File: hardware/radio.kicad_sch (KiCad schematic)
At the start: 25 parts, among them J1 105450-0101, J2 Conn_01x02, J3 Conn_01x02, U1 TP4056, U2 ESP32-WROOM-32, U3 TPS5432, U4 MAX98357

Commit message: schematic
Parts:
- added C13, C15, C16: 100n, Capacitor_SMD:C_0603_1608Metric, symbol Device:C
- added C14: 10u, Capacitor_SMD:C_1206_3216Metric, symbol Device:C
- added J4: Conn_01x04, Connector_PinHeader_2.54mm:PinHeader_1x04_P2.54mm_Vertical, symbol Connector_Generic:Conn_01x04
- added Q1: Q_PMOS_DGS, Package_TO_SOT_SMD:SOT-23, symbol Device:Q_PMOS_DGS
- added Q2: Q_NMOS_DGS, Package_TO_SOT_SMD:SOT-23, symbol Device:Q_NMOS_DGS
- added R5, R8: 10k, Resistor_SMD:R_0603_1608Metric, symbol Device:R
- added R6: 100k, Resistor_SMD:R_0603_1608Metric, symbol Device:R
- added R7: 330k, Resistor_SMD:R_0603_1608Metric, symbol Device:R
- added SW1: SW_BOOT, symbol Switch:SW_Push
- added SW2: SW_RST, symbol Switch:SW_Push
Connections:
- net +3V3: now also C13.2, C14.2, J4.1 (Pin_1), R5.1
- net +BATT: now also Q1.3 (S), R8.1
- net -BATT: now also C13.1, C14.1, C15.1, C16.2, J4.4 (Pin_4), Q2.3 (S), R7.2, SW1.2, SW2.1
- net at U2.25 (IO0): now also C16.1, SW1.1
- net at U2.3 (EN): now also C15.2, R5.2, SW2.2
- net at U2.34 (RXD0/IO3): now also J4.3 (Pin_3)
- net at U2.35 (TXD0/IO1): now also J4.2 (Pin_2)
- new net: Q1.1 (D), R6.1
- new net: Q1.2 (G), Q2.1 (D), R8.2
- new net ADC IN: R6.2, R7.1
- new net ADC_ENABLE: Q2.2 (G)
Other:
- note added: "ADC circuit to prevent leakage current through the resistor divider. Divider reduces the maximum voltage from 4,2 V to ~3,2 V"
- note added: "TODO: * SHUTDOWN CIRCUIT * CONNECT DISPLAY AND DAC/AMP TO ESP32 * CONNECT USB TO ESP32, ADD CC RESISTORS * ADD BUTTONS, ROTARY ENCODER"
- note added: "UART"
- moved on the sheet: C10, C9, DISP1, J3, U2, U4

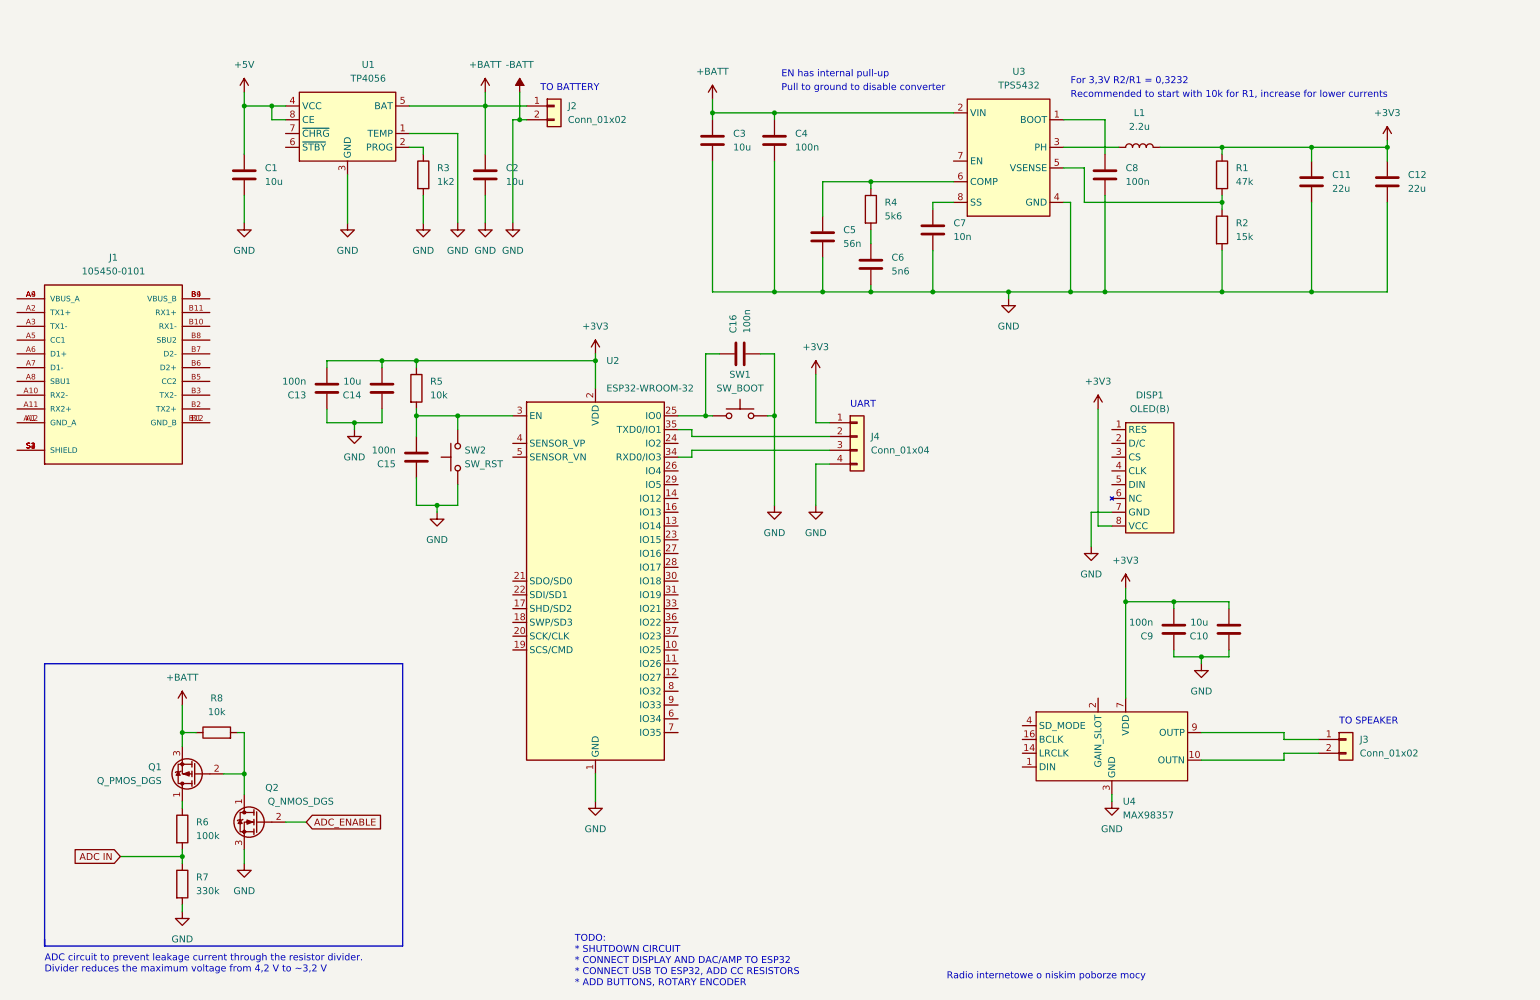
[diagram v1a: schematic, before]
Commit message: added to schematic: rotary encoder, buttons, USB-C receptacle CC resistors
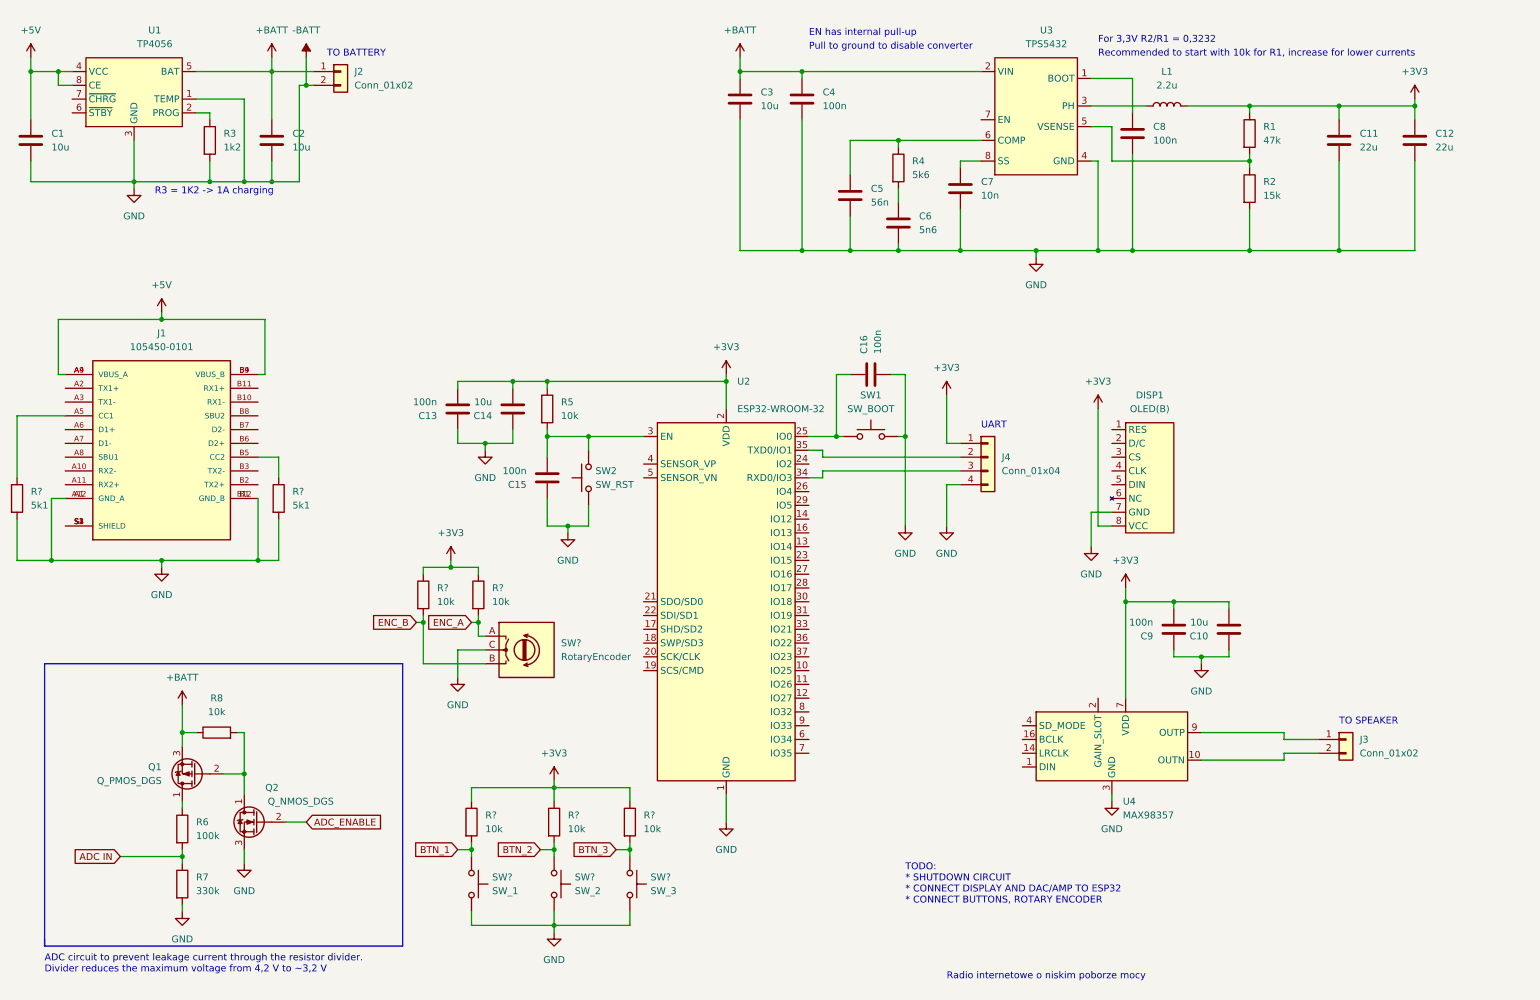
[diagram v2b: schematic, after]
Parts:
- added R? (x5): 10k, Resistor_SMD:R_0603_1608Metric, symbol Device:R
- added R? (x2): 5k1, Resistor_SMD:R_0603_1608Metric, symbol Device:R
- added SW?: SW_1, symbol Switch:SW_Push
- added SW?: RotaryEncoder, symbol Device:RotaryEncoder
- added SW?: SW_2, symbol Switch:SW_Push
- added SW?: SW_3, symbol Switch:SW_Push
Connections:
- net +3V3: now also R?.1, R?.1, R?.1, R?.1, R?.1
- net +5V: now also J1.A4 (VBUS_A), J1.A9 (VBUS_A), J1.B4 (VBUS_B), J1.B9 (VBUS_B)
- net -BATT: now also J1.A1 (GND_A), J1.A12 (GND_A), J1.B1 (GND_B), J1.B12 (GND_B), R?.2, R?.2, SW?.2, SW?.2, SW?.2, SW?.C
- net at J1.A5 (CC1): now also R?.1
- net at J1.B5 (CC2): now also R?.1
- new net BTN_1: R?.2, SW?.1
- new net BTN_2: R?.2, SW?.1
- new net BTN_3: R?.2, SW?.1
- new net ENC_A: R?.2, SW?.A
- new net ENC_B: R?.2, SW?.B
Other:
- note added: "R3 = 1K2 -> 1A charging"
- note added: "TODO: * SHUTDOWN CIRCUIT * CONNECT DISPLAY AND DAC/AMP TO ESP32 * CONNECT BUTTONS, ROTARY ENCODER"
- note removed: "TODO: * SHUTDOWN CIRCUIT * CONNECT DISPLAY AND DAC/AMP TO ESP32 * CONNECT USB TO ESP32, ADD CC RESISTORS * ADD BUTTONS, ROTARY ENCODER"
- moved on the sheet: C1, C11, C12, C13, C14, C15, C16, C2, C3, C4, C5, C6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

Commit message: added shutdown circuit
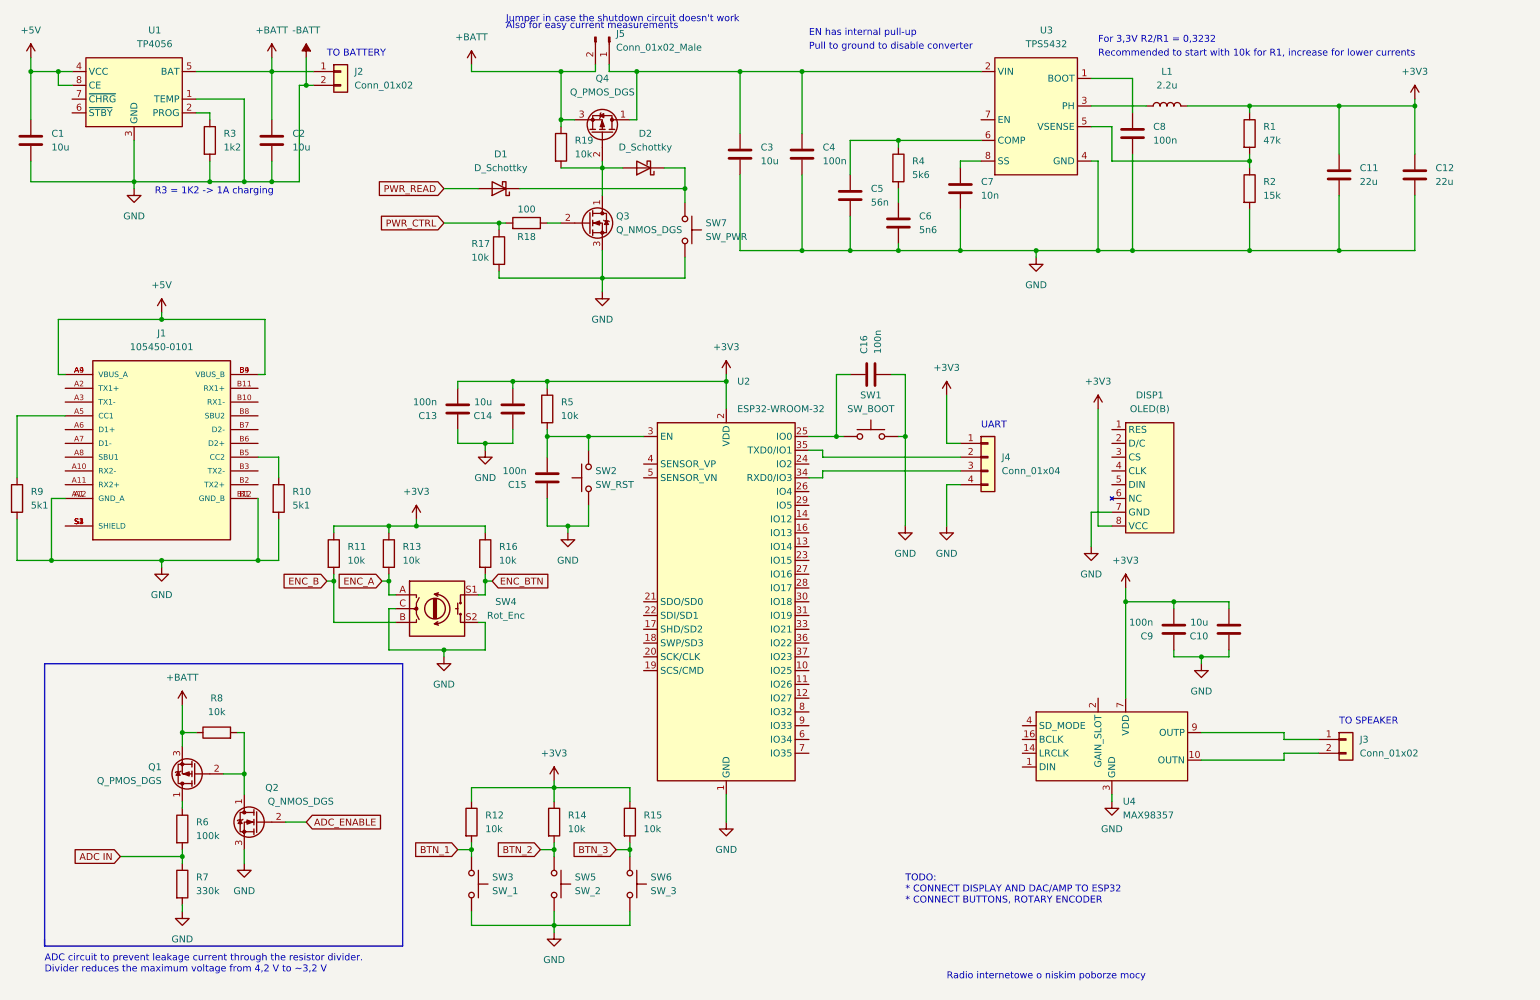
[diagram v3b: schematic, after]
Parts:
- removed SW?: RotaryEncoder, symbol Device:RotaryEncoder
- added D1, D2: D_Schottky, Diode_SMD:D_SMA, symbol Device:D_Schottky
- added J5: Conn_01x02_Male, Connector_PinHeader_2.54mm:PinHeader_1x02_P2.54mm_Horizontal, symbol Connector:Conn_01x02_Male
- added Q3: Q_NMOS_DGS, Package_TO_SOT_SMD:SOT-23, symbol Device:Q_NMOS_DGS
- added Q4: Q_PMOS_DGS, Package_TO_SOT_SMD:SOT-23, symbol Device:Q_PMOS_DGS
- added R16, R17, R19: 10k, Resistor_SMD:R_0603_1608Metric, symbol Device:R
- added R18: 100, Resistor_SMD:R_0603_1608Metric, symbol Device:R
- added SW4: Rot_Enc, Rotary_Encoder:RotaryEncoder_Alps_EC12E-Switch_Vertical_H20mm_CircularMountingHoles, symbol Device:RotaryEncoder_Switch
- added SW7: SW_PWR, symbol Switch:SW_Push
- gave numbers to parts that had none: 10
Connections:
- net +3V3: now also R16.1
- net +BATT: now also J5.2 (Pin_2), Q4.3 (S), R19.1; no longer C3.1, C4.1, U3.2 (VIN)
- net -BATT: now also Q3.3 (S), R17.2, SW4.C, SW4.S2, SW7.1
- net ENC_A: now also SW4.A
- net ENC_B: now also SW4.B
- new net: C3.1, C4.1, J5.1 (Pin_1), Q4.1 (D), U3.2 (VIN)
- new net: D2.2 (A), Q3.1 (D), Q4.2 (G), R19.2
- new net: D1.1 (K), D2.1 (K), SW7.2
- new net: Q3.2 (G), R18.1
- new net ENC_BTN: R16.2, SW4.S1
- new net PWR_CTRL: R17.1, R18.2
- new net PWR_READ: D1.2 (A)
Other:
- note added: "Also for easy current measurements"
- note added: "Jumper in case the shutdown circuit doesn't work"
- note added: "TODO: * CONNECT DISPLAY AND DAC/AMP TO ESP32 * CONNECT BUTTONS, ROTARY ENCODER"
- note removed: "TODO: * SHUTDOWN CIRCUIT * CONNECT DISPLAY AND DAC/AMP TO ESP32 * CONNECT BUTTONS, ROTARY ENCODER"
- moved on the sheet: C11, C12, C3, C4, R11, R13

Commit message: comments
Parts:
- added R20: 10k, Resistor_SMD:R_0603_1608Metric, symbol Device:R
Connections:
- net +3V3: now also R20.1
- net PWR_READ: now also R20.2
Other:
- note added: "For full voltage range configure ADC to 11dB attenuation"
- note added: "Optional in case internal pull-up is too weak"
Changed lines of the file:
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@@
   (junction (at 60.96 113.03) (diameter 0) (color 0 0 0 0)
   )
+  (junction (at 97.79 44.45) (diameter 0) (color 0 0 0 0)
+  )
   (junction (at 105.41 50.8) (diameter 0) (color 0 0 0 0)
   )
@@
     (stroke (width 0) (type default) (color 0 0 0 0))
   )
+  (wire (pts (xy 97.79 34.29) (xy 97.79 35.56))
+    (stroke (width 0) (type default) (color 0 0 0 0))
+  )
   (wire (pts (xy 114.3 80.01) (xy 114.3 81.28))
     (stroke (width 0) (type default) (color 0 0 0 0))
@@
     (stroke (width 0) (type default) (color 0 0 0 0))
   )
+  (wire (pts (xy 97.79 43.18) (xy 97.79 44.45))
+    (stroke (width 0) (type default) (color 0 0 0 0))
+  )
   (wire (pts (xy 139.7 57.15) (xy 139.7 60.96))
     (stroke (width 0) (type default) (color 0 0 0 0))
@@
     (stroke (width 0) (type default) (color 0 0 0 0))
   )
+  (wire (pts (xy 97.79 44.45) (xy 101.6 44.45))
+    (stroke (width 0) (type default) (color 0 0 0 0))
+  )
   (wire (pts (xy 170.18 35.56) (xy 179.07 35.56))
     (stroke (width 0) (type default) (color 0 0 0 0))
@@
     (stroke (width 0) (type default) (color 0 0 0 0))
   )
-  (wire (pts (xy 95.25 44.45) (xy 101.6 44.45))
+  (wire (pts (xy 95.25 44.45) (xy 97.79 44.45))
     (stroke (width 0) (type default) (color 0 0 0 0))
   )
@@
     (effects (font (size 1.27 1.27)) (justify left bottom))
   )
+  (text "Optional in case\ninternal pull-up \nis too weak" (at 80.01 38.1 0)
+    (effects (font (size 1.27 1.27)) (justify left bottom))
+  )
   (text "TO BATTERY" (at 73.66 20.32 0)
     (effects (font (size 1.27 1.27)) (justify left bottom))
@@
   (text "ADC circuit to prevent leakage current through the resistor divider.\nDivider reduces the maximum voltage from 4,2 V to ~3,2 V"
     (at 21.59 189.23 0)
+    (effects (font (size 1.27 1.27)) (justify left bottom))
+  )
+  (text "For full voltage range configure ADC to 11dB attenuation"
+    (at 21.59 191.77 0)
     (effects (font (size 1.27 1.27)) (justify left bottom))
   )
@@
     (pin "2")
   )
+  (symbol (lib_id "power:+3V3") (at 97.79 34.29 0) (unit 1)
+    (in_bom yes) (on_board yes) (fields_autoplaced)
+    (property "Reference" "#PWR0124" (id 0) (at 97.79 38.1 0)
+      (effects (font (size 1.27 1.27)) hide)
+    )
+    (property "Value" "+3V3" (id 1) (at 97.79 29.21 0))
+    (property "Footprint" "" (id 2) (at 97.79 34.29 0)
+      (effects (font (size 1.27 1.27)) hide)
+    )
+    (property "Datasheet" "" (id 3) (at 97.79 34.29 0)
+      (effects (font (size 1.27 1.27)) hide)
+    )
+    (pin "1")
+  )
   (symbol (lib_id "Device:R") (at 129.54 161.29 0) (unit 1)
     (in_bom yes) (on_board yes) (fields_autoplaced)
@@
     )
     (property "Datasheet" "~" (id 3) (at 229.87 125.73 0)
+      (effects (font (size 1.27 1.27)) hide)
+    )
+    (pin "1")
+    (pin "2")
+  )
+  (symbol (lib_id "Device:R") (at 97.79 39.37 0) (unit 1)
+    (in_bom yes) (on_board yes)
+    (property "Reference" "R20" (id 0) (at 92.71 38.1 0)
+      (effects (font (size 1.27 1.27)) (justify left))
+    )
+    (property "Value" "10k" (id 1) (at 92.71 40.64 0)
+      (effects (font (size 1.27 1.27)) (justify left))
+    )
+    (property "Footprint" "Resistor_SMD:R_0603_1608Metric" (id 2) (at 96.012 39.37 90)
+      (effects (font (size 1.27 1.27)) hide)
+    )
+    (property "Datasheet" "~" (id 3) (at 97.79 39.37 0)
       (effects (font (size 1.27 1.27)) hide)
     )
@@
       (reference "#PWR0123") (unit 1) (value "GND") (footprint "")
     )
+    (path "/0c98ec6d-5605-4ae5-b17f-f4dc21bdc12f"
+      (reference "#PWR0124") (unit 1) (value "+3V3") (footprint "")
+    )
     (path "/31276b67-1ce3-42d3-a55d-ef9419463436"
       (reference "C1") (unit 1) (value "10u") (footprint "Capacitor_SMD:C_1206_3216Metric")
@@
       (reference "R19") (unit 1) (value "10k") (footprint "Resistor_SMD:R_0603_1608Metric")
     )
+    (path "/44b6afa7-5f7c-4171-bba2-97a4b6f894a2"
+      (reference "R20") (unit 1) (value "10k") (footprint "Resistor_SMD:R_0603_1608Metric")
+    )
     (path "/395dc202-ab89-4816-9a78-379ff056d9ef"
